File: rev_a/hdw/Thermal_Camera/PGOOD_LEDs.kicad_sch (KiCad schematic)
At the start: 29 parts, among them U1501 74LVC1G97

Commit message: lots of schematic progress
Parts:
- C2703: renamed from C?; footprint Capacitors_SMD:C_0603 -> (none); Digi-Key PN 1276-1935-1-ND -> (none); display_footprint 0603 -> (none)
- C? (x6): renamed from C1501; footprint Capacitors_SMD:C_0603 -> (none); Digi-Key PN 1276-1935-1-ND -> (none); display_footprint 0603 -> (none)
- D2703: renamed from D?; footprint LEDs:LED_0603 -> (none)
- D? (x6): renamed from D1501; footprint LEDs:LED_0603 -> (none); Digi-Key PN 754-1121-1-ND -> (none)
- R2704: renamed from R?; footprint Resistors_SMD:R_0603 -> (none); Digi-Key PN 541-1.00KHCT-ND -> (none); Wattage 1/10W -> (none); display_footprint 0603 -> (none)
- R? (x6): renamed from R1502; footprint Resistors_SMD:R_0603 -> (none); Digi-Key PN 541-1.00KHCT-ND -> (none); Wattage 1/10W -> (none); display_footprint 0603 -> (none)
- R?: renamed from R1501; footprint Resistors_SMD:R_0603 -> (none); Digi-Key PN 541-10.0KHCT-ND -> (none); Wattage 1/10W -> (none); display_footprint 0603 -> (none)
- gave numbers to parts that had none: 2
- renumbered U1501 to U?

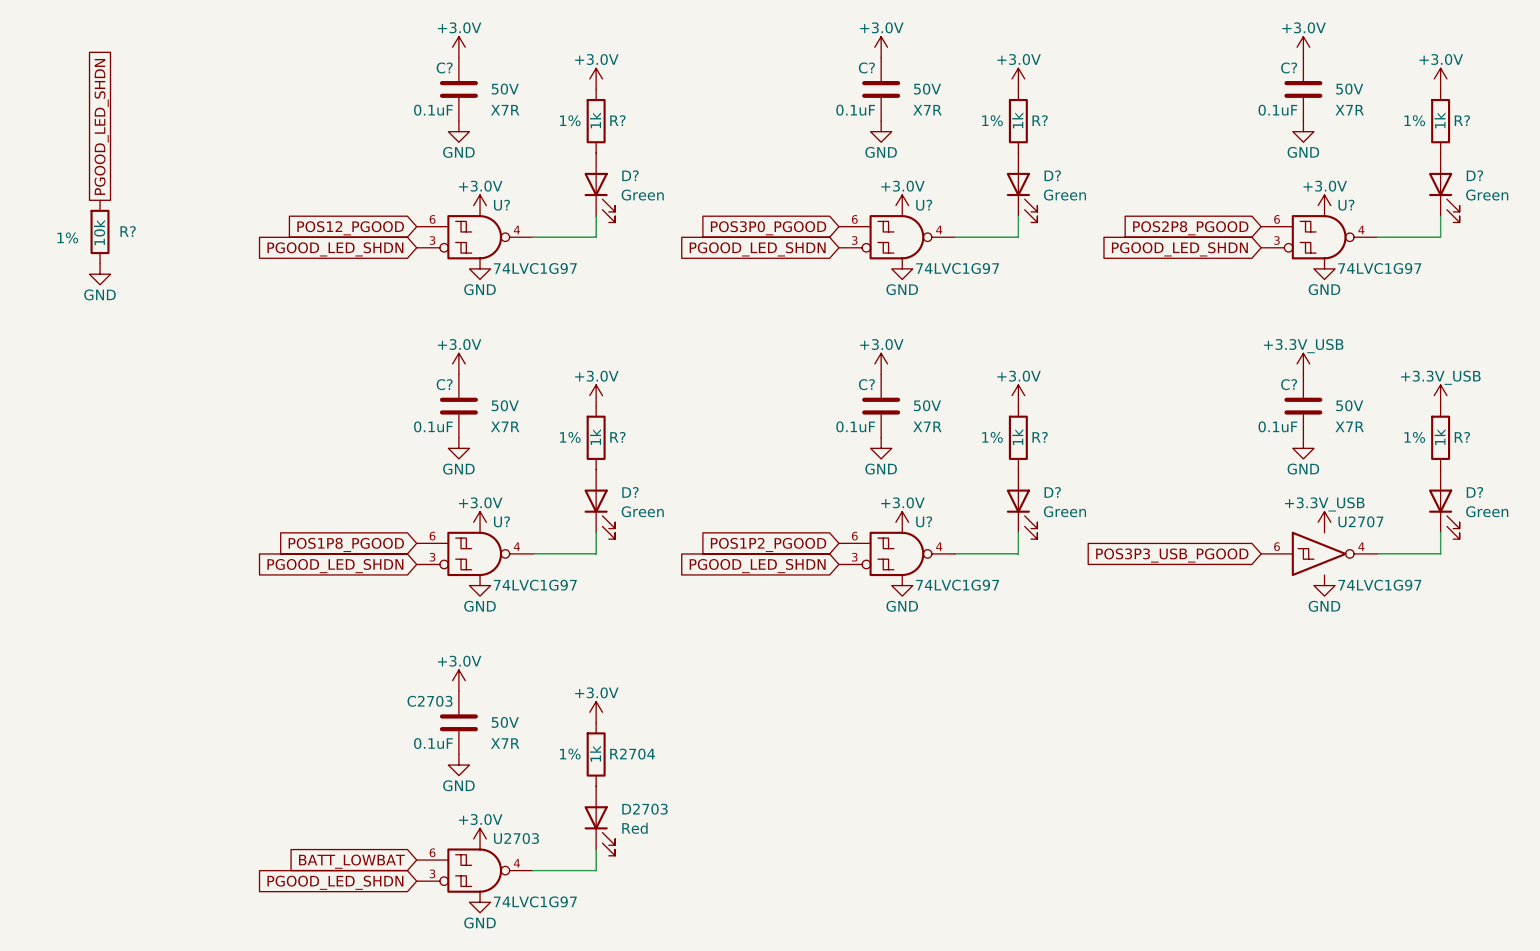
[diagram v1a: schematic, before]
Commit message: assigned a ton of footprints
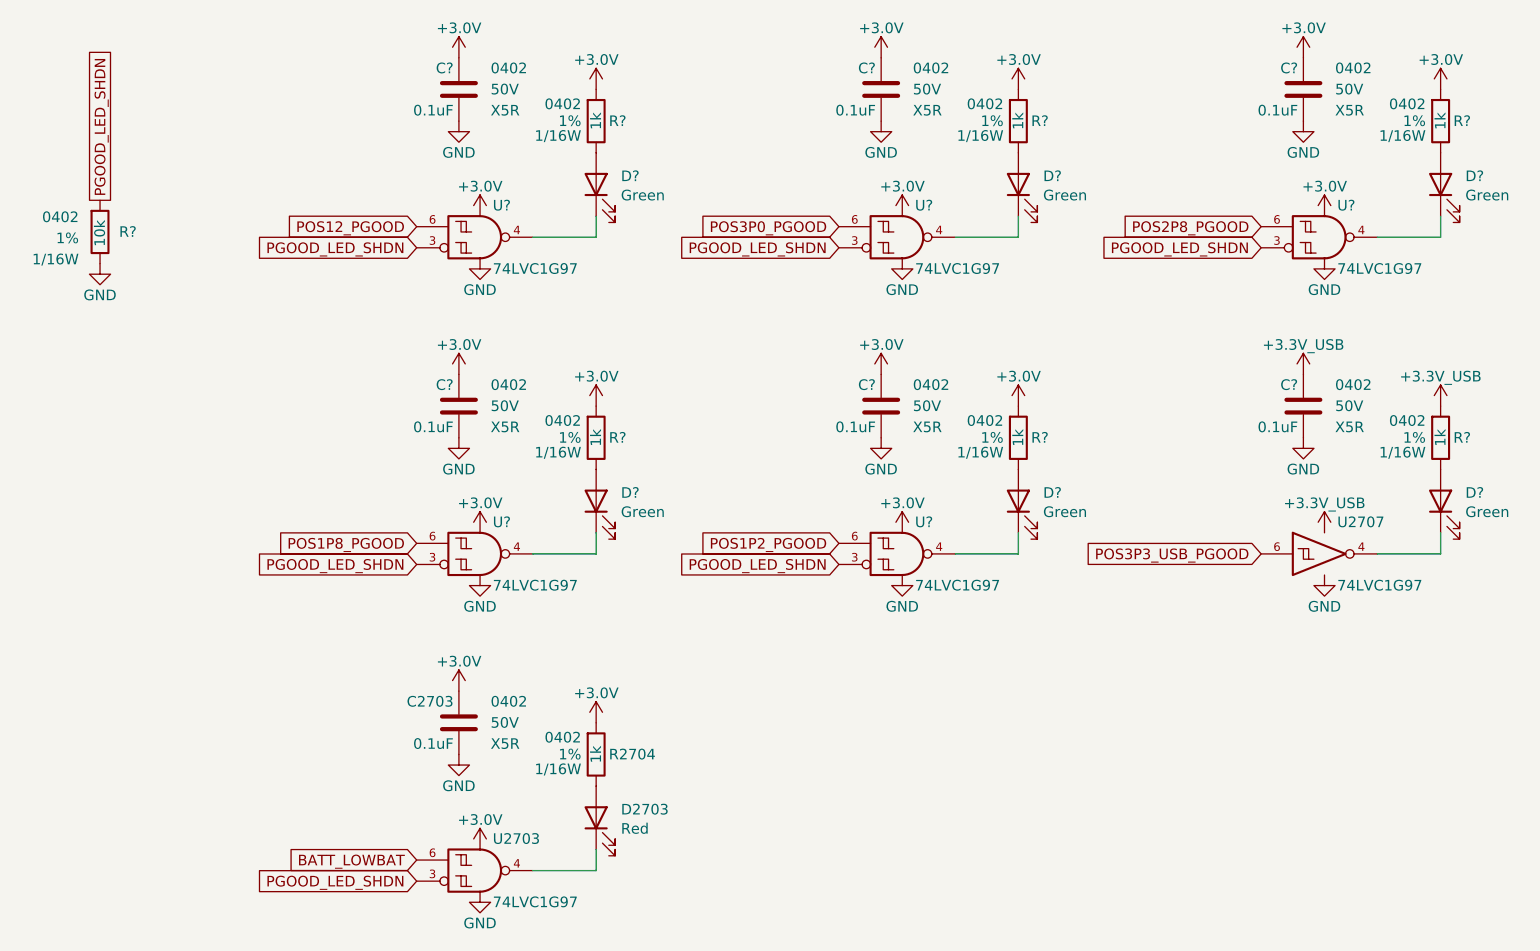
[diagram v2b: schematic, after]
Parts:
- C2703, C? (x6): footprint (none) -> Capacitors_SMD:C_0402; Dielectric X7R -> X5R; display_footprint (none) -> 0402
- D2703, D? (x6): footprint (none) -> LEDs:LED_0402
- R2704, R? (x7): footprint (none) -> Resistors_SMD:R_0402; Wattage (none) -> 1/16W; display_footprint (none) -> 0402
- U2707: Digi-Key PN (none) -> 296-15582-1-ND
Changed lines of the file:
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@@
 			)
 		)
-		(property "Footprint" ""
+		(property "Footprint" "Resistors_SMD:R_0402"
 			(at 187.96 43.18 0)
 			(effects
@@
 			)
 		)
-		(property "display_footprint" ""
+		(property "display_footprint" "0402"
 			(at 186.182 41.148 0)
 			(effects
@@
 			)
 		)
-		(property "Wattage" ""
+		(property "Wattage" "1/16W"
 			(at 186.182 44.958 0)
 			(effects
@@
 			)
 		)
-		(property "Footprint" ""
+		(property "Footprint" "Resistors_SMD:R_0402"
 			(at 86.36 119.38 0)
 			(effects
@@
 			)
 		)
-		(property "display_footprint" ""
+		(property "display_footprint" "0402"
 			(at 84.582 117.348 0)
 			(effects
@@
 			)
 		)
-		(property "Wattage" ""
+		(property "Wattage" "1/16W"
 			(at 84.582 121.158 0)
 			(effects
@@
 			)
 		)
+		(property "Digi-Key PN" "296-15582-1-ND"
+			(at 173.99 95.25 0)
+			(effects
+				(font
+					(size 1.27 1.27)
+				)
+				(hide yes)
+			)
+		)
 		(pin "1"
 		)
@@
 			)
 		)
-		(property "Footprint" ""
+		(property "Footprint" "Resistors_SMD:R_0402"
 			(at 137.16 81.28 0)
 			(effects
@@
 			)
 		)
-		(property "display_footprint" ""
+		(property "display_footprint" "0402"
 			(at 135.382 79.248 0)
 			(effects
@@
 			)
 		)
-		(property "Wattage" ""
+		(property "Wattage" "1/16W"
 			(at 135.382 83.058 0)
 			(effects
@@
 			)
 		)
-		(property "Footprint" ""
+		(property "Footprint" "Capacitors_SMD:C_0402"
 			(at 119.6848 43.18 0)
 			(effects
@@
 			)
 		)
-		(property "display_footprint" ""
+		(property "display_footprint" "0402"
 			(at 124.46 36.83 0)
 			(effects
@@
 			)
 		)
-		(property "Dielectric" "X7R"
+		(property "Dielectric" "X5R"
 			(at 124.46 41.91 0)
 			(effects
@@
 			)
 		)
-		(property "Footprint" ""
+		(property "Footprint" "LEDs:LED_0402"
 			(at 86.36 127 0)
 			(effects
@@
 			)
 		)
-		(property "Footprint" ""
+		(property "Footprint" "LEDs:LED_0402"
 			(at 137.16 88.9 0)
 			(effects
@@
 			)
 		)
-		(property "Footprint" ""
+		(property "Footprint" "Resistors_SMD:R_0402"
 			(at 86.36 81.28 0)
 			(effects
@@
 			)
 		)
-		(property "display_footprint" ""
+		(property "display_footprint" "0402"
 			(at 84.582 79.248 0)
 			(effects
@@
 			)
 		)
-		(property "Wattage" ""
+		(property "Wattage" "1/16W"
 			(at 84.582 83.058 0)
 			(effects
@@
 			)
 		)
-		(property "Footprint" ""
+		(property "Footprint" "Capacitors_SMD:C_0402"
 			(at 119.6848 81.28 0)
 			(effects
@@
 			)
 		)
-		(property "display_footprint" ""
+		(property "display_footprint" "0402"
 			(at 124.46 74.93 0)
 			(effects
@@
 			)
 		)
-		(property "Dielectric" "X7R"
+		(property "Dielectric" "X5R"
 			(at 124.46 80.01 0)
 			(effects
@@
 			)
 		)
-		(property "Footprint" ""
+		(property "Footprint" "LEDs:LED_0402"
 			(at 187.96 50.8 0)
 			(effects
@@
 			)
 		)
-		(property "Footprint" ""
+		(property "Footprint" "Resistors_SMD:R_0402"
 			(at 187.96 81.28 0)
 			(effects
@@
 			)
 		)
-		(property "display_footprint" ""
+		(property "display_footprint" "0402"
 			(at 186.182 79.248 0)
 			(effects
@@
 			)
 		)
-		(property "Wattage" ""
+		(property "Wattage" "1/16W"
 			(at 186.182 83.058 0)
 			(effects
@@
 			)
 		)
-		(property "Footprint" ""
+		(property "Footprint" "Capacitors_SMD:C_0402"
 			(at 170.4848 81.28 0)
 			(effects
@@
 			)
 		)
-		(property "display_footprint" ""
+		(property "display_footprint" "0402"
 			(at 175.26 74.93 0)
 			(effects
@@
 			)
 		)
-		(property "Dielectric" "X7R"
+		(property "Dielectric" "X5R"
 			(at 175.26 80.01 0)
 			(effects
@@
 			)
 		)
-		(property "Footprint" ""
+		(property "Footprint" "Resistors_SMD:R_0402"
 			(at 137.16 43.18 0)
 			(effects
@@
 			)
 		)
-		(property "display_footprint" ""
+		(property "display_footprint" "0402"
 			(at 135.382 41.148 0)
 			(effects
@@
 			)
 		)
-		(property "Wattage" ""
+		(property "Wattage" "1/16W"
 			(at 135.382 44.958 0)
 			(effects
@@
 			)
 		)
-		(property "Footprint" ""
+		(property "Footprint" "LEDs:LED_0402"
 			(at 187.96 88.9 0)
 			(effects
@@
 			)
 		)
-		(property "Footprint" ""
+		(property "Footprint" "Capacitors_SMD:C_0402"
 			(at 170.4848 43.18 0)
 			(effects
@@
 			)
 		)
-		(property "display_footprint" ""
+		(property "display_footprint" "0402"
 			(at 175.26 36.83 0)
 			(effects
@@
 			)
 		)
-		(property "Dielectric" "X7R"
+		(property "Dielectric" "X5R"
 			(at 175.26 41.91 0)
 			(effects
@@
 			)
 		)
-		(property "Footprint" ""
+		(property "Footprint" "Capacitors_SMD:C_0402"
 			(at 68.8848 81.28 0)
 			(effects
@@
 			)
 		)
-		(property "display_footprint" ""
+		(property "display_footprint" "0402"
 			(at 73.66 74.93 0)
 			(effects
@@
 			)
 		)
-		(property "Dielectric" "X7R"
+		(property "Dielectric" "X5R"
 			(at 73.66 80.01 0)
 			(effects
@@
 			)
 		)
-		(property "Footprint" ""
+		(property "Footprint" "LEDs:LED_0402"
 			(at 86.36 88.9 0)
 			(effects
@@
 			)
 		)
-		(property "Footprint" ""
+		(property "Footprint" "LEDs:LED_0402"
 			(at 137.16 50.8 0)
 			(effects
@@
 			)
 		)
-		(property "Footprint" ""
+		(property "Footprint" "Resistors_SMD:R_0402"
 			(at 26.67 56.515 0)
 			(effects
@@
 			)
 		)
-		(property "display_footprint" ""
+		(property "display_footprint" "0402"
 			(at 24.13 54.737 0)
 			(effects
@@
 			)
 		)
-		(property "Wattage" ""
+		(property "Wattage" "1/16W"
 			(at 24.13 59.817 0)
 			(effects
@@
 			)
 		)
-		(property "Footprint" ""
+		(property "Footprint" "Capacitors_SMD:C_0402"
 			(at 68.8848 43.18 0)
 			(effects
@@
 			)
 		)
-		(property "display_footprint" ""
+		(property "display_footprint" "0402"
 			(at 73.66 36.83 0)
 			(effects
@@
 			)
 		)
-		(property "Dielectric" "X7R"
+		(property "Dielectric" "X5R"
 			(at 73.66 41.91 0)
 			(effects
@@
 			)
 		)
-		(property "Footprint" ""
+		(property "Footprint" "LEDs:LED_0402"
 			(at 86.36 50.8 0)
 			(effects
@@
 			)
 		)
-		(property "Footprint" ""
+		(property "Footprint" "Resistors_SMD:R_0402"
 			(at 86.36 43.18 0)
 			(effects
@@
 			)
 		)
-		(property "display_footprint" ""
+		(property "display_footprint" "0402"
 			(at 84.582 41.148 0)
 			(effects
@@
 			)
 		)
-		(property "Wattage" ""
+		(property "Wattage" "1/16W"
 			(at 84.582 44.958 0)
 			(effects
@@
 			)
 		)
-		(property "Footprint" ""
+		(property "Footprint" "Capacitors_SMD:C_0402"
 			(at 68.8848 119.38 0)
 			(effects
@@
 			)
 		)
-		(property "display_footprint" ""
+		(property "display_footprint" "0402"
 			(at 73.66 113.03 0)
 			(effects
@@
 			)
 		)
-		(property "Dielectric" "X7R"
+		(property "Dielectric" "X5R"
 			(at 73.66 118.11 0)
 			(effects

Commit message: assigned some part numbers
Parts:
- C2703, C? (x6): Digi-Key PN (none) -> 490-10697-1-ND
- D2703: Digi-Key PN (none) -> VLMS1500-GS08CT-ND
- D? (x6): Digi-Key PN (none) -> 1497-1219-1-ND
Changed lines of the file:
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@@
 			)
 		)
-		(property "Digi-Key PN" ""
+		(property "Digi-Key PN" "490-10697-1-ND"
 			(at 109.855 26.67 0)
 			(effects
@@
 			)
 		)
-		(property "Digi-Key PN" ""
+		(property "Digi-Key PN" "VLMS1500-GS08CT-ND"
 			(at 246.888 258.064 0)
 			(effects
@@
 			)
 		)
-		(property "Digi-Key PN" ""
+		(property "Digi-Key PN" "1497-1219-1-ND"
 			(at 297.688 219.964 0)
 			(effects
@@
 			)
 		)
-		(property "Digi-Key PN" ""
+		(property "Digi-Key PN" "490-10697-1-ND"
 			(at 109.855 64.77 0)
 			(effects
@@
 			)
 		)
-		(property "Digi-Key PN" ""
+		(property "Digi-Key PN" "1497-1219-1-ND"
 			(at 348.488 181.864 0)
 			(effects
@@
 			)
 		)
-		(property "Digi-Key PN" ""
+		(property "Digi-Key PN" "490-10697-1-ND"
 			(at 160.655 64.77 0)
 			(effects
@@
 			)
 		)
-		(property "Digi-Key PN" ""
+		(property "Digi-Key PN" "1497-1219-1-ND"
 			(at 348.488 219.964 0)
 			(effects
@@
 			)
 		)
-		(property "Digi-Key PN" ""
+		(property "Digi-Key PN" "490-10697-1-ND"
 			(at 160.655 26.67 0)
 			(effects
@@
 			)
 		)
-		(property "Digi-Key PN" ""
+		(property "Digi-Key PN" "490-10697-1-ND"
 			(at 59.055 64.77 0)
 			(effects
@@
 			)
 		)
-		(property "Digi-Key PN" ""
+		(property "Digi-Key PN" "1497-1219-1-ND"
 			(at 246.888 219.964 0)
 			(effects
@@
 			)
 		)
-		(property "Digi-Key PN" ""
+		(property "Digi-Key PN" "1497-1219-1-ND"
 			(at 297.688 181.864 0)
 			(effects
@@
 			)
 		)
-		(property "Digi-Key PN" ""
+		(property "Digi-Key PN" "490-10697-1-ND"
 			(at 59.055 26.67 0)
 			(effects
@@
 			)
 		)
-		(property "Digi-Key PN" ""
+		(property "Digi-Key PN" "1497-1219-1-ND"
 			(at 246.888 181.864 0)
 			(effects
@@
 			)
 		)
-		(property "Digi-Key PN" ""
+		(property "Digi-Key PN" "490-10697-1-ND"
 			(at 59.055 102.87 0)
 			(effects

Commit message: assigned resistor part numbers
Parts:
- R2704, R? (x6): Digi-Key PN (none) -> RMCF0402FT1K00CT-ND
- R?: Digi-Key PN (none) -> RMCF0402FT10K0CT-ND
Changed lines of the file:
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@@
 			)
 		)
-		(property "Digi-Key PN" ""
+		(property "Digi-Key PN" "RMCF0402FT1K00CT-ND"
 			(at 180.34 33.02 0)
 			(effects
@@
 			)
 		)
-		(property "Digi-Key PN" ""
+		(property "Digi-Key PN" "RMCF0402FT1K00CT-ND"
 			(at 78.74 109.22 0)
 			(effects
@@
 			)
 		)
-		(property "Digi-Key PN" ""
+		(property "Digi-Key PN" "RMCF0402FT1K00CT-ND"
 			(at 129.54 71.12 0)
 			(effects
@@
 			)
 		)
-		(property "Digi-Key PN" ""
+		(property "Digi-Key PN" "RMCF0402FT1K00CT-ND"
 			(at 78.74 71.12 0)
 			(effects
@@
 			)
 		)
-		(property "Digi-Key PN" ""
+		(property "Digi-Key PN" "RMCF0402FT1K00CT-ND"
 			(at 180.34 71.12 0)
 			(effects
@@
 			)
 		)
-		(property "Digi-Key PN" ""
+		(property "Digi-Key PN" "RMCF0402FT1K00CT-ND"
 			(at 129.54 33.02 0)
 			(effects
@@
 			)
 		)
-		(property "Digi-Key PN" ""
+		(property "Digi-Key PN" "RMCF0402FT10K0CT-ND"
 			(at 19.05 46.355 0)
 			(effects
@@
 			)
 		)
-		(property "Digi-Key PN" ""
+		(property "Digi-Key PN" "RMCF0402FT1K00CT-ND"
 			(at 78.74 33.02 0)
 			(effects
